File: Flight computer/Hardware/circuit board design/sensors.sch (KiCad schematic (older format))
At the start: 7 parts, among them U7 MPU-9150, U8 MS5607-02BA

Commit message: Got the GPS wired up with the MAX-M8C.
I wired up the MCU to the GPS as well. Sensors are also wired up to the I2C line.

TODO:
-make everything run on 3.3V
- work out the pyro charges and drivers
many more.
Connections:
- net labels added: +3.3V
- net labels removed: +1V8
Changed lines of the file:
@@
 	2550 4500 2550 3550
-$Comp
-L power:+1V8 #PWR0114
-U 1 1 5D882794
-P 3300 3800
-F 0 "#PWR0114" H 3300 3650 50  0001 C CNN
-F 1 "+1V8" H 3315 3973 50  0000 C CNN
-F 2 "" H 3300 3800 50  0001 C CNN
-F 3 "" H 3300 3800 50  0001 C CNN
-	1    3300 3800
-	1    0    0    -1
-$EndComp
 $Comp
 L Device:C_Small C77
@@
 	1    0    0    -1
 $EndComp
-$Comp
-L power:+1V8 #PWR0117
-U 1 1 5D88F8DD
-P 3650 900
-F 0 "#PWR0117" H 3650 750 50  0001 C CNN
-F 1 "+1V8" H 3665 1073 50  0000 C CNN
-F 2 "" H 3650 900 50  0001 C CNN
-F 3 "" H 3650 900 50  0001 C CNN
-	1    3650 900
-	1    0    0    -1
-$EndComp
 Wire Wire Line
 	3300 3850 3300 4000
@@
 NoConn ~ 3950 2100
 NoConn ~ 3950 2200
-$Comp
-L power:+1V8 #PWR0122
-U 1 1 5D8A0F6B
-P 2950 900
-F 0 "#PWR0122" H 2950 750 50  0001 C CNN
-F 1 "+1V8" H 2965 1073 50  0000 C CNN
-F 2 "" H 2950 900 50  0001 C CNN
-F 3 "" H 2950 900 50  0001 C CNN
-	1    2950 900
-	1    0    0    -1
-$EndComp
 Wire Wire Line
 	3350 1500 3350 1000
@@
 Text HLabel 1200 3550 0    50   BiDi ~ 0
 SENS_SCL
+$Comp
+L power:+3.3V #PWR?
+U 1 1 5D6AE039
+P 3300 3800
+F 0 "#PWR?" H 3300 3650 50  0001 C CNN
+F 1 "+3.3V" H 3315 3973 50  0000 C CNN
+F 2 "" H 3300 3800 50  0001 C CNN
+F 3 "" H 3300 3800 50  0001 C CNN
+	1    3300 3800
+	1    0    0    -1
+$EndComp
+$Comp
+L power:+3.3V #PWR?
+U 1 1 5D6AF037
+P 2950 900
+F 0 "#PWR?" H 2950 750 50  0001 C CNN
+F 1 "+3.3V" H 2965 1073 50  0000 C CNN
+F 2 "" H 2950 900 50  0001 C CNN
+F 3 "" H 2950 900 50  0001 C CNN
+	1    2950 900
+	1    0    0    -1
+$EndComp
+$Comp
+L power:+3.3V #PWR?
+U 1 1 5D6B0691
+P 3650 900
+F 0 "#PWR?" H 3650 750 50  0001 C CNN
+F 1 "+3.3V" H 3665 1073 50  0000 C CNN
+F 2 "" H 3650 900 50  0001 C CNN
+F 3 "" H 3650 900 50  0001 C CNN
+	1    3650 900
+	1    0    0    -1
+$EndComp
 $EndSCHEMATC

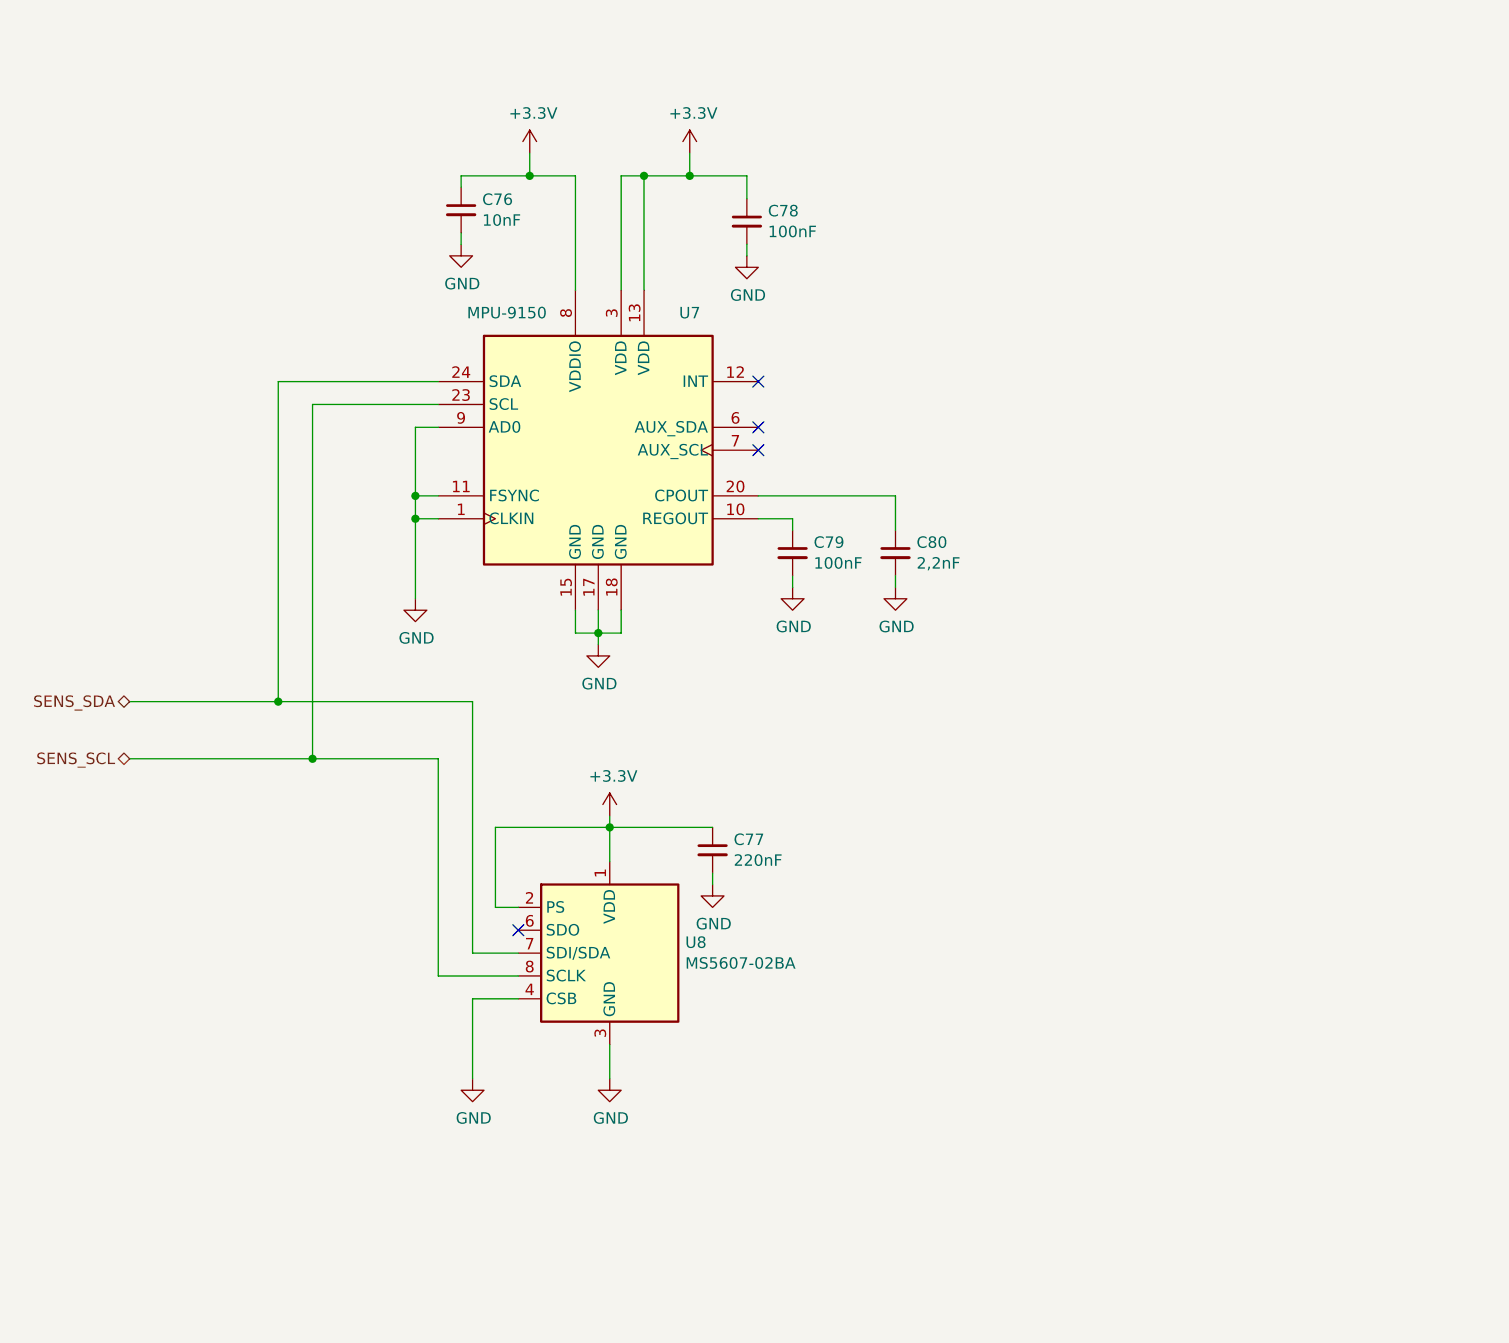
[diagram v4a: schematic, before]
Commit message: Replaced acclerometer with BMI088 6 dof sensor
-replaced the schematic symbol
-replaced the footprint. added a local copy
-wired up the BMI088
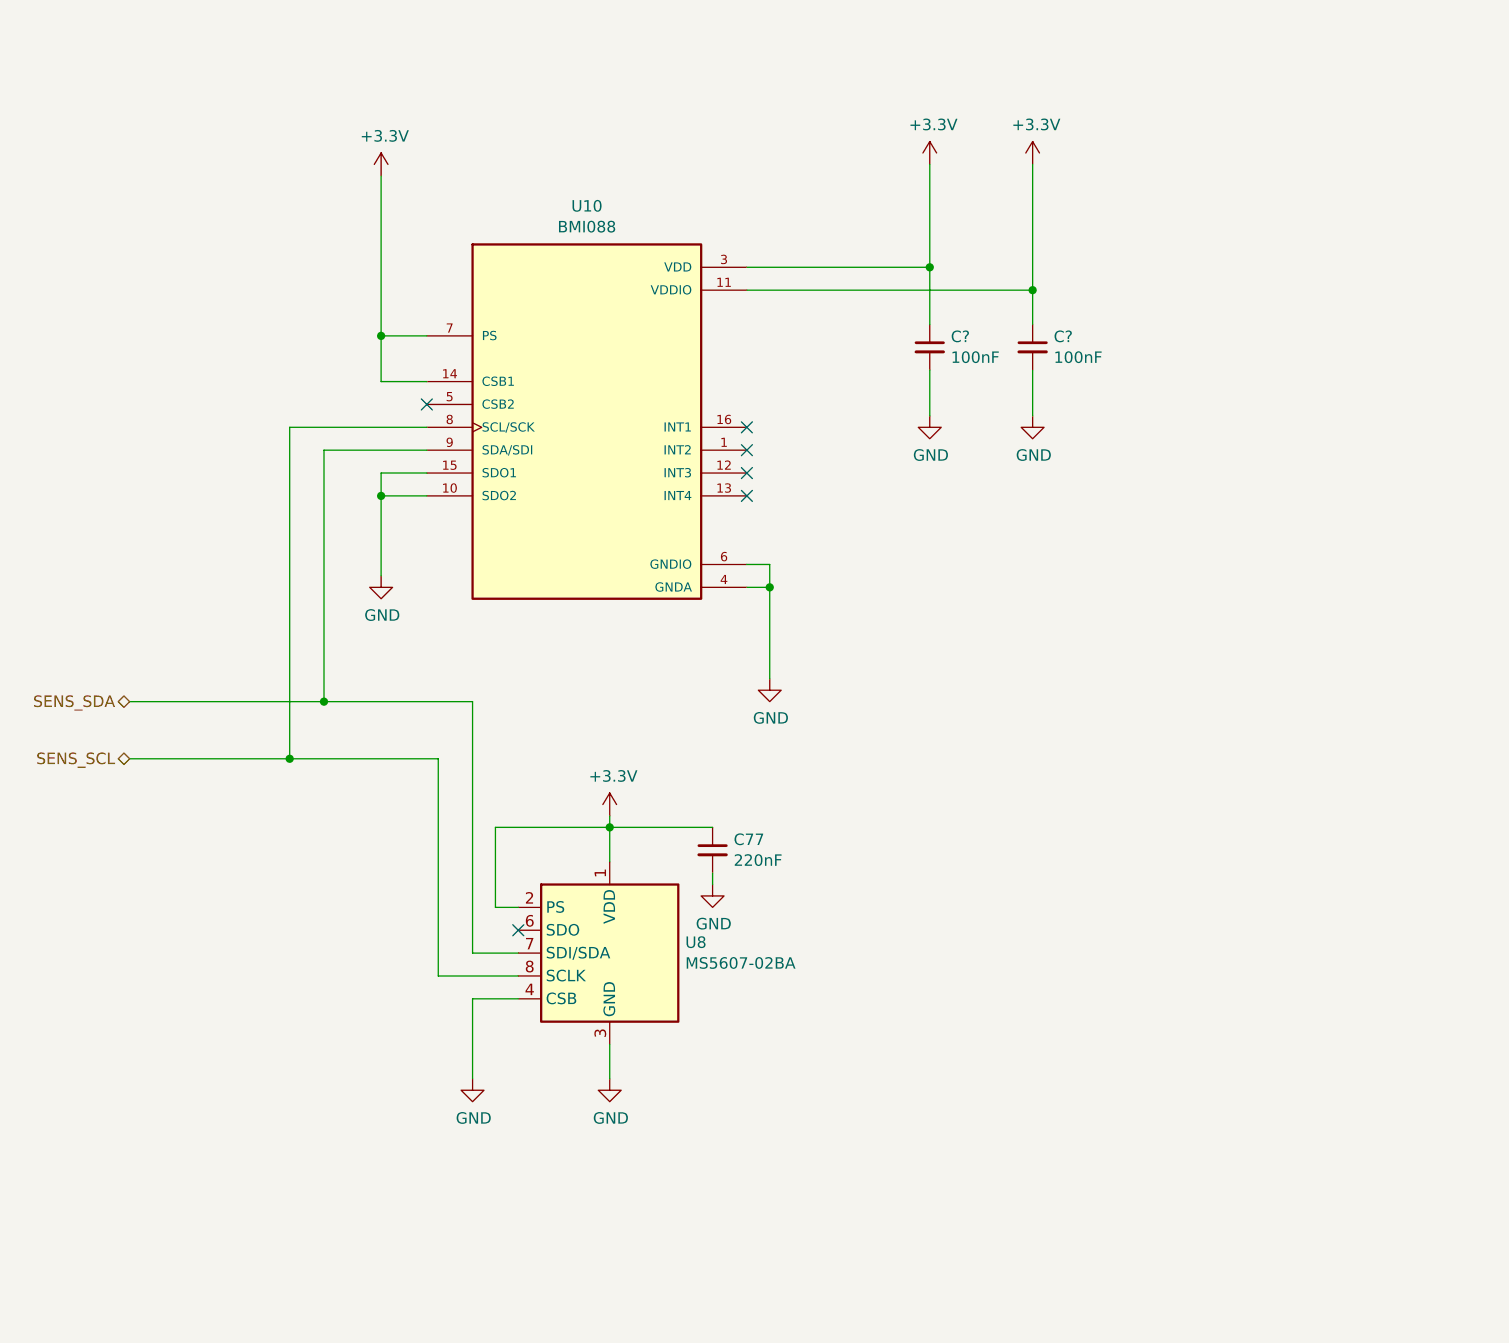
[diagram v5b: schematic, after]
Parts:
- removed C76: 10nF, Capacitor_SMD:C_0402_1005Metric, symbol Device:C_Small
- removed C78, C79: 100nF, Capacitor_SMD:C_0603_1608Metric, symbol Device:C_Small
- removed C80: 2,2nF, Capacitor_SMD:C_0402_1005Metric, symbol Device:C_Small
- removed U7: MPU-9150, Sensor_Motion:InvenSense_QFN-24_4x4mm_P0.5mm, symbol Sensor_Motion:MPU-9150
- added C? (x2): 100nF, Capacitor_SMD:C_0402_1005Metric, symbol Device:C_Small
- added U10: BMI088, fligh computer:PQFN50P450X300X100-16N, symbol BMI088:BMI088
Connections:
- net +3V3: now also C?.1, C?.1, U10.11 (VDDIO), U10.14 (CSB1), U10.3 (VDD), U10.7 (PS)
- net GND: now also C?.2, C?.2, U10.10 (SDO2), U10.15 (SDO1), U10.4 (GNDA), U10.6 (GNDIO)
- net SENS_SCL: now also U10.8 (SCL/SCK)
- net SENS_SDA: now also U10.9 (SDA/SDI)
- no-connect marks 4 -> 6

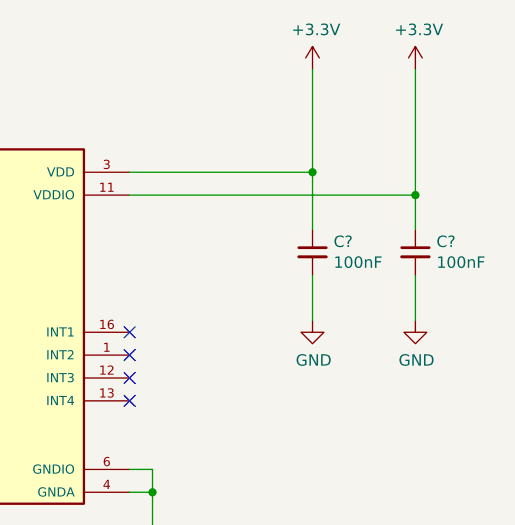
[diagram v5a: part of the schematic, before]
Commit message: changed all the paths for the schematic, footprints to local versions
so that it will not break when others access from another computer
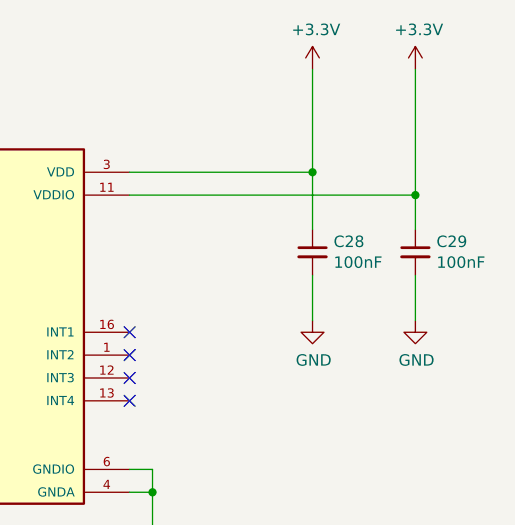
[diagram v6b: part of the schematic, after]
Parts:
- U10: footprint fligh computer:PQFN50P450X300X100-16N -> flight-computer:PQFN50P450X300X100-16N
- gave numbers to parts that had none: 2

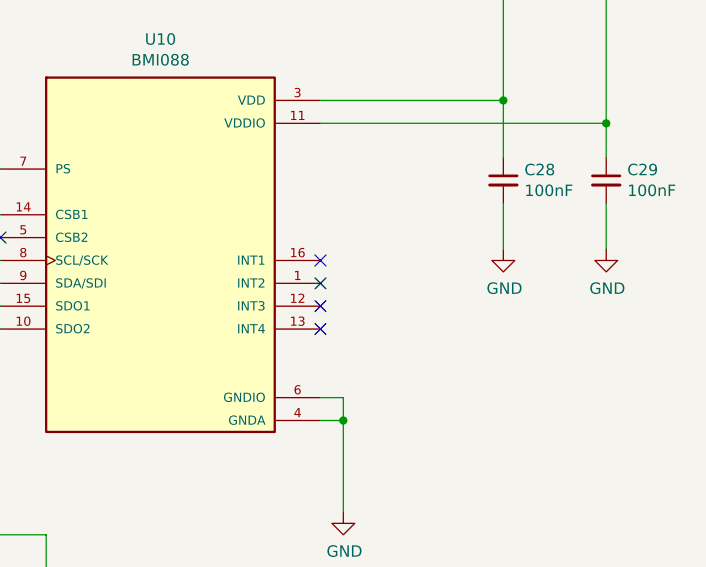
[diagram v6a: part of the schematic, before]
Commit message: Wired the GYRO Ready and ACCL ready interrupt pins
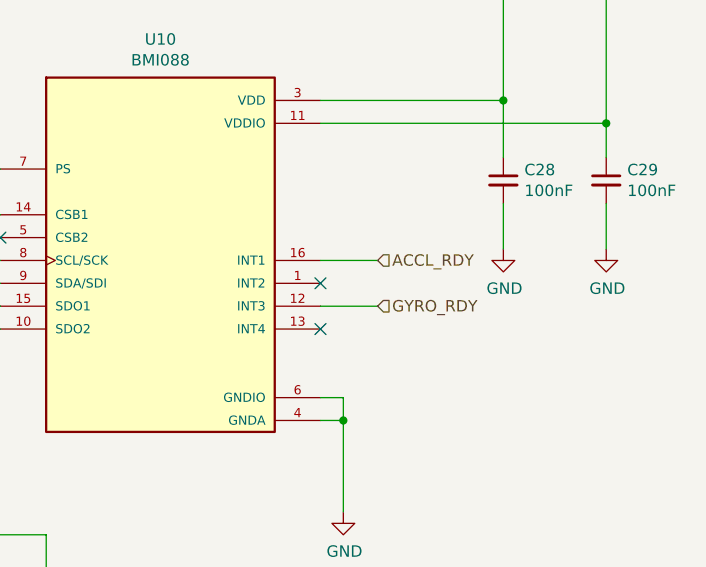
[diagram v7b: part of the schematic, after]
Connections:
- net GYRO_RDY: now reaches U10.12 (INT3)
- net ACCL_RDY: now reaches U10.16 (INT1)
- no-connect marks 6 -> 4
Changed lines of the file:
@@
 	3900 1500 5150 1500
 NoConn ~ 3900 2400
-NoConn ~ 3900 2300
 NoConn ~ 3900 2200
-NoConn ~ 3900 2100
 $Comp
 L Sensor_Pressure:MS5607-02BA U8
@@
 	1    0    0    -1
 $EndComp
+Text HLabel 4150 2100 2    50   Input ~ 0
+ACCL_RDY
+Wire Wire Line
+	3900 2100 4150 2100
+Text HLabel 4150 2300 2    50   Input ~ 0
+GYRO_RDY
+Wire Wire Line
+	3900 2300 4150 2300
 $EndSCHEMATC
